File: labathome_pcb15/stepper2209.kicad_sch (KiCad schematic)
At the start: 45 parts, among them J24 K1, J30 K1, J31 K1, U14 TMC2209, U19 TMC2209, U20 TMC2209

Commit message: Merged and fixed (WIP)
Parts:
- R83, R84: footprint Resistor_SMD:R_1206_3216Metric -> Resistor_SMD:R_0805_2012Metric
- renumbered C67 to C120
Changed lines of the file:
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@@
 		(on_board yes)
 		(dnp no)
-		(property "Reference" "C67"
+		(property "Reference" "C120"
 			(at 130.048 25.654 0)
 			(effects
@@
 			(project "labathome_pcb15"
 				(path "/e4d6926a-1a8b-424d-97c4-66b6ad87e4ac/17ae4001-8623-479a-8825-80beba02b053"
-					(reference "C67")
+					(reference "C120")
 					(unit 1)
 				)
@@
 			)
 		)
-		(property "Footprint" "Resistor_SMD:R_1206_3216Metric"
+		(property "Footprint" "Resistor_SMD:R_0805_2012Metric"
 			(at 66.802 83.82 90)
 			(effects
@@
 			)
 		)
-		(property "Footprint" "Resistor_SMD:R_1206_3216Metric"
+		(property "Footprint" "Resistor_SMD:R_0805_2012Metric"
 			(at 74.422 83.82 90)
 			(effects
@@
 		(dnp no)
 		(fields_autoplaced yes)
-		(property "Reference" "#PWR0139"
+		(property "Reference" "#PWR0192"
 			(at 50.8 93.98 0)
 			(effects
@@
 			(project ""
 				(path "/e4d6926a-1a8b-424d-97c4-66b6ad87e4ac/17ae4001-8623-479a-8825-80beba02b053"
-					(reference "#PWR0139")
+					(reference "#PWR0192")
 					(unit 1)
 				)

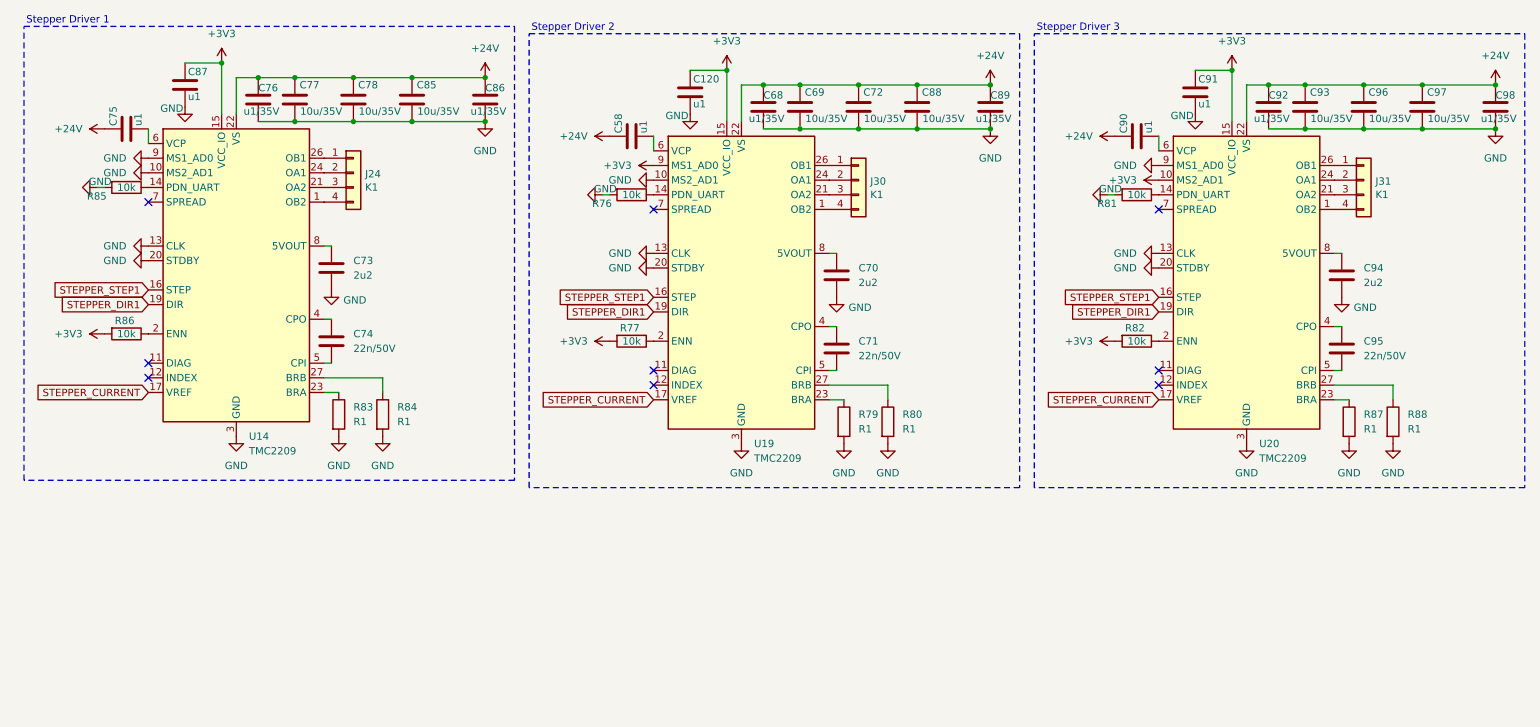
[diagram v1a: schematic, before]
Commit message: Added stepper, no DRC errors, not yet optimized
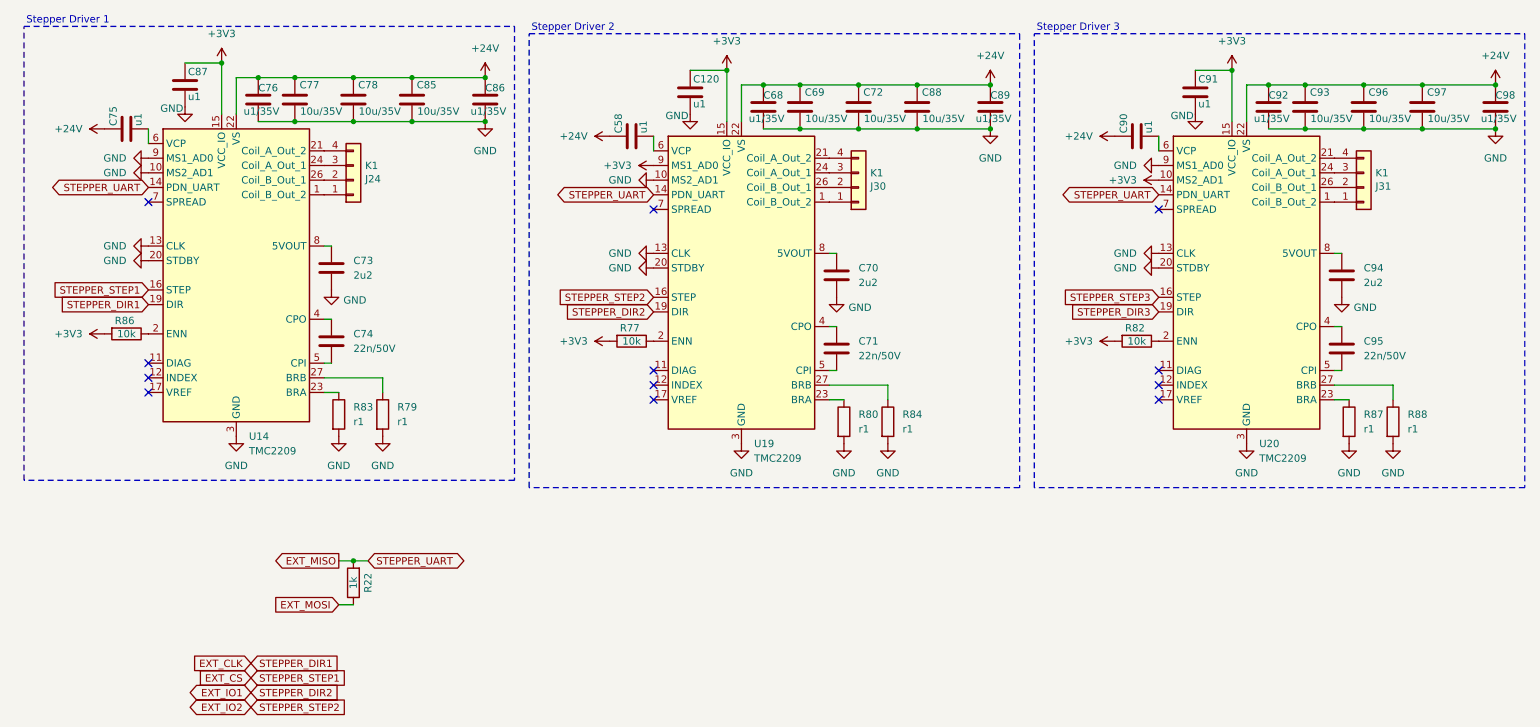
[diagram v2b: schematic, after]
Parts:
- removed R76, R81, R85: 10k, Resistor_SMD:R_0201_0603Metric, symbol Device:R
- added R22: 1k, Resistor_SMD:R_0402_1005Metric, symbol Device:R
- R79, R80, R87, R88: value R1 -> r1; footprint Resistor_SMD:R_1206_3216Metric -> Resistor_SMD:R_2010_5025Metric
- R83, R84: value R1 -> r1; footprint Resistor_SMD:R_0805_2012Metric -> Resistor_SMD:R_2010_5025Metric
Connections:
- net at U20.1 (Coil_B_Out_2): now also J31.1 (Pin_1); no longer J31.4 (Pin_4)
- net EXT_MISO: now reaches U20.14 (PDN_UART)
- net EXT_MISO: now also U14.14 (PDN_UART), U19.14 (PDN_UART), R22.2
- net at U20.21 (Coil_A_Out_2): now also J31.4 (Pin_4); no longer J31.3 (Pin_3)
- net at U20.24 (Coil_A_Out_1): now also J31.3 (Pin_3); no longer J31.2 (Pin_2)
- net at U20.26 (Coil_B_Out_1): now also J31.2 (Pin_2); no longer J31.1 (Pin_1)
- net at U14.1 (Coil_B_Out_2): now also J24.1 (Pin_1); no longer J24.4 (Pin_4)
- net at U14.21 (Coil_A_Out_2): now also J24.4 (Pin_4); no longer J24.3 (Pin_3)
- net at U14.24 (Coil_A_Out_1): now also J24.3 (Pin_3); no longer J24.2 (Pin_2)
- net at U14.26 (Coil_B_Out_1): now also J24.2 (Pin_2); no longer J24.1 (Pin_1)
- net at U14.27 (BRB): now also R79.1; no longer R84.1
- net at U19.23 (BRA): now also R80.1; no longer R79.1
- net at J30.1 (Pin_1): now also U19.1 (Coil_B_Out_2); no longer U19.26 (OB1)
- net at J30.2 (Pin_2): now also U19.26 (Coil_B_Out_1); no longer U19.24 (OA1)
- net at J30.3 (Pin_3): now also U19.24 (Coil_A_Out_1); no longer U19.21 (OA2)
- net at J30.4 (Pin_4): now also U19.21 (Coil_A_Out_2); no longer U19.1 (OB2)
- net at U19.27 (BRB): now also R84.1; no longer R80.1
- removed net STEPPER_CURRENT: U14.17 (VREF), U19.17 (VREF), U20.17 (VREF)
- removed net STEPPER_DIR1: U14.19 (DIR), U19.19 (DIR), U20.19 (DIR)
- removed net STEPPER_STEP1: U14.16 (STEP), U19.16 (STEP), U20.16 (STEP)
- new net EXT_CLK: U14.19 (DIR)
- new net EXT_CS: U14.16 (STEP)
- new net EXT_IO1: U19.19 (DIR)
- new net EXT_IO2: U19.16 (STEP)
- new net EXT_MOSI: R22.1
- new net STEPPER_DIR3: U20.19 (DIR)
- new net STEPPER_STEP3: U20.16 (STEP)
- no-connect marks 9 -> 12
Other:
- moved on the sheet: J24, J30, J31

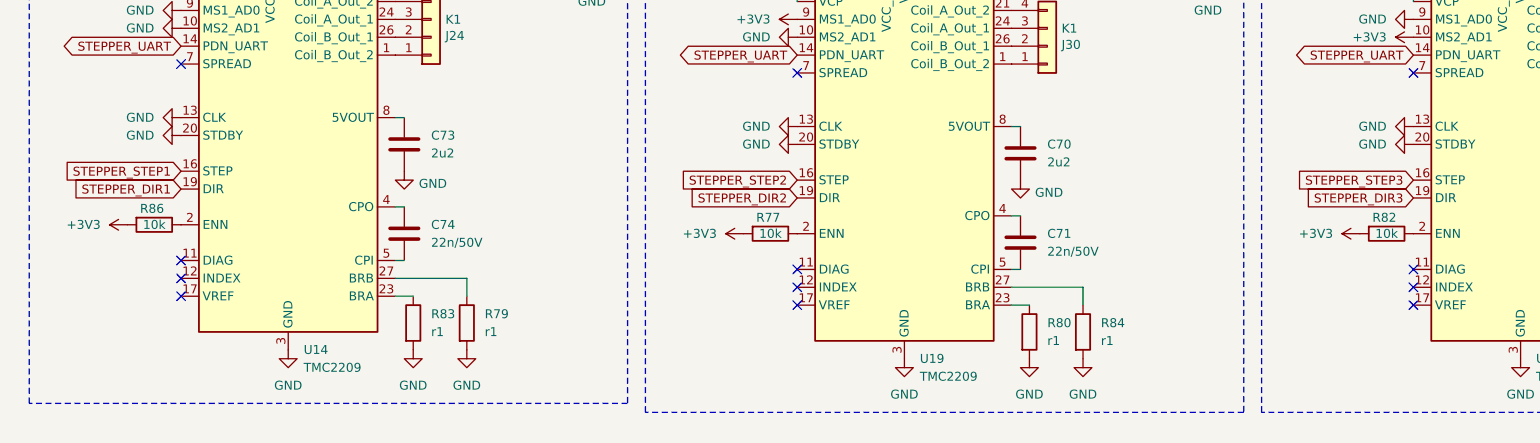
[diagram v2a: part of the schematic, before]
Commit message: Layout improvement; use common enable signal for steppers
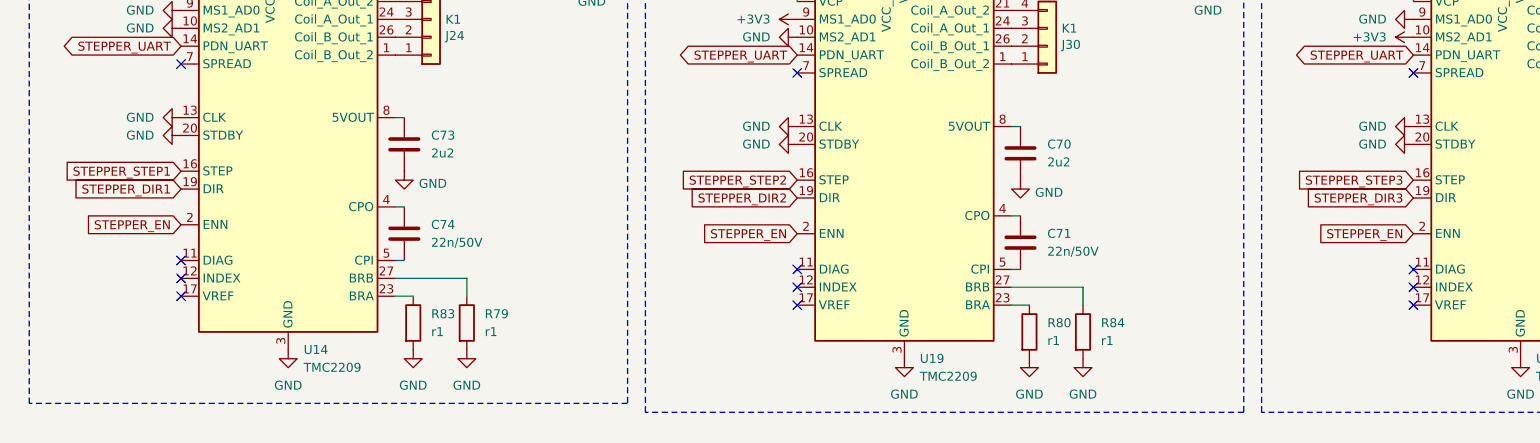
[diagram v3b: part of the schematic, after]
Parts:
- removed R77, R82, R86: 10k, Resistor_SMD:R_0201_0603Metric, symbol Device:R
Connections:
- net STEPPER_EN: now reaches U20.2 (ENN)
- net STEPPER_EN: now also U14.2 (ENN), U19.2 (ENN)
